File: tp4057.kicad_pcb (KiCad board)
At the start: 2 copper layers, 62.7 x 33.3 mm, 28 parts, among them J1 Conn_02x01, J2 Conn_02x01, J3 USB_C_Receptacle_PowerOnly_6P, J4 Conn_02x01, U1 TP4057, U2 TP4057, U3 TP4057

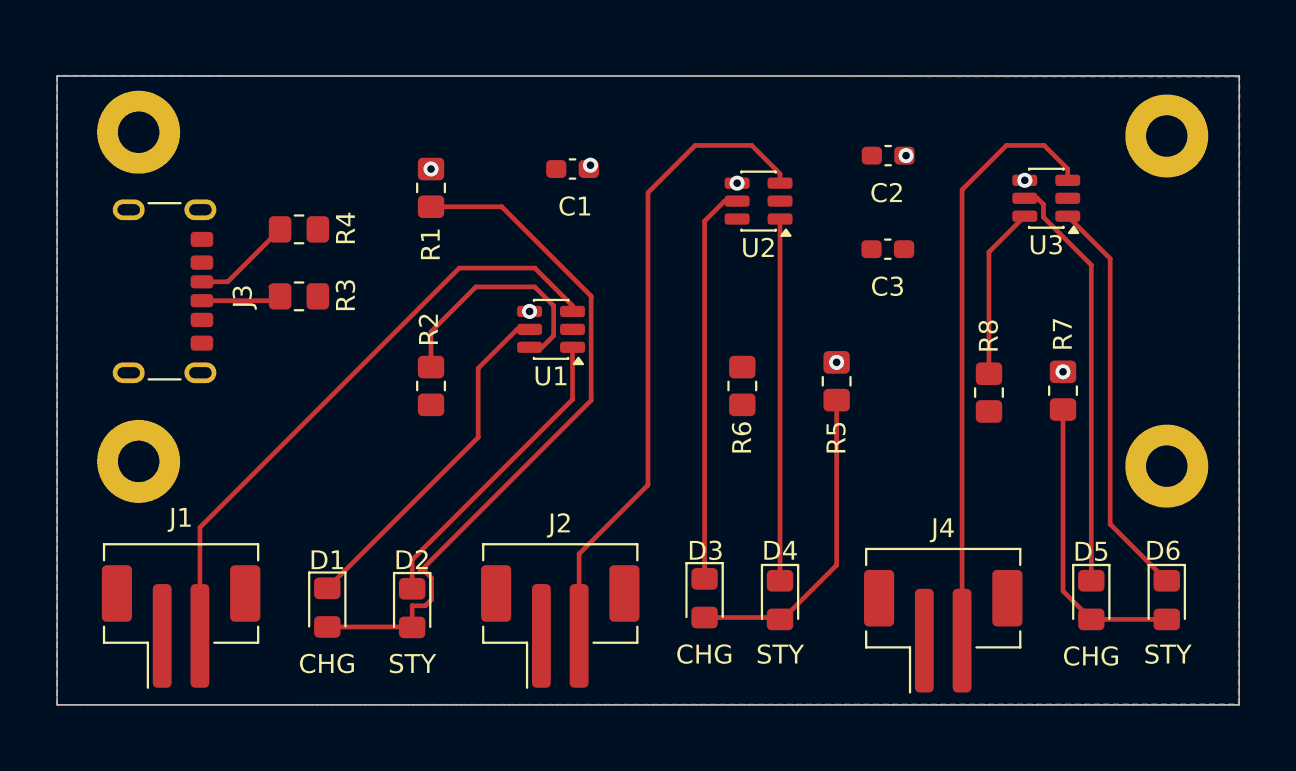
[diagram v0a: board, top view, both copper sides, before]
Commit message: Fixed VCC plane not connecting (misplaced vias), changed trace thickness, routed remaining components
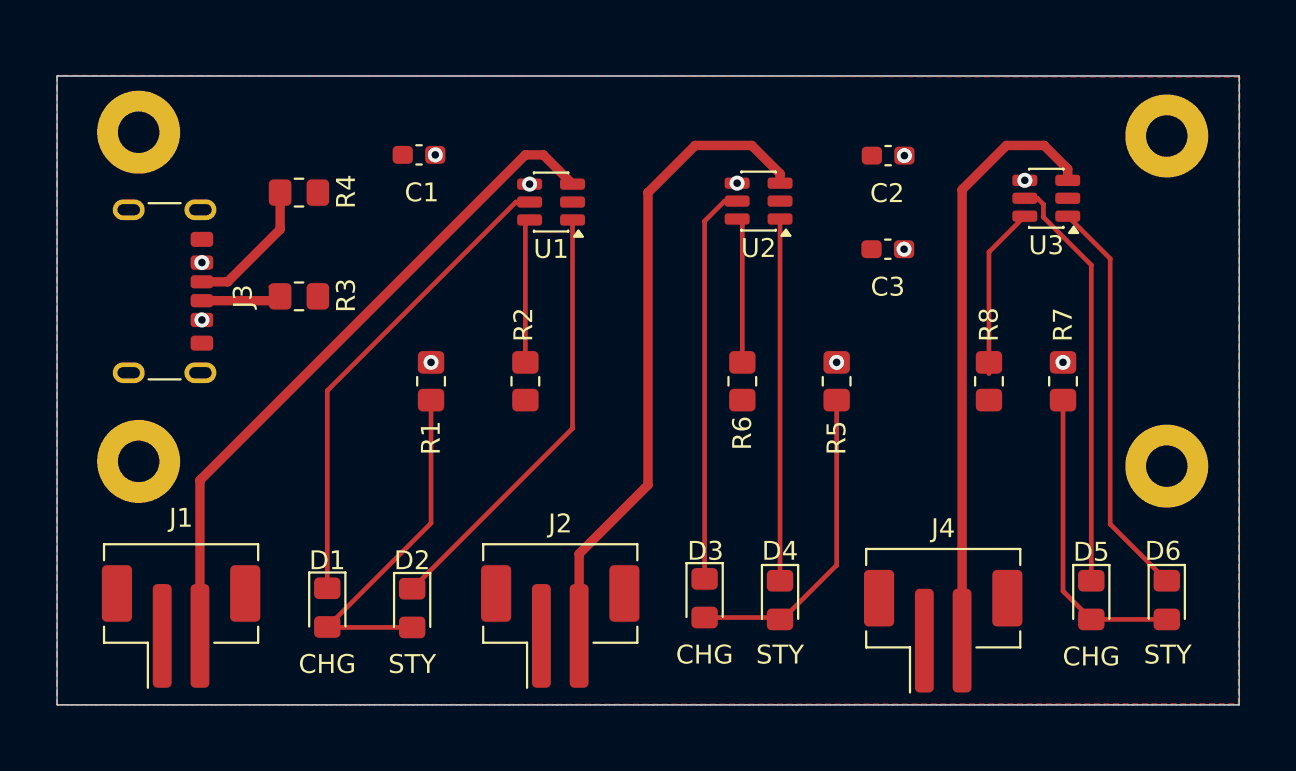
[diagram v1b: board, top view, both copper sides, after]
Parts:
- moved R1 10.2 mm to (158.0, 134.5)
- moved C1 8.17 mm to (157.4, 122.5)
- moved U1 6.75 mm to (164.4, 125.0)
- moved R2 5.01 mm to (163.0, 134.5)
- moved R4 1.95 mm to (151.0, 124.5)
- moved R8 0.60 mm to (187.6, 134.5)
- moved R7 0.50 mm to (191.5, 134.5)
- moved R6 0.25 mm to (174.5, 134.5)
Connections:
- H1 pad 1: GND -> unconnected-(H1-Pad1)
- H2 pad 1: GND -> unconnected-(H2-Pad1)
- H3 pad 1: GND -> unconnected-(H3-Pad1)
- H4 pad 1: GND -> unconnected-(H4-Pad1)
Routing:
- net Net-(D1-A): track 37.6 -> 18.8 mm
- net Net-(U2-PROG): track 0.00 -> 7.96 mm
- net Net-(D1-K): track 18.6 -> 25.3 mm
- net Net-(D2-K): track 16.3 -> 23.1 mm
- net Net-(U1-PROG): track 13.5 -> 7.64 mm
- net Net-(J1-Pin_2): track 32.3 -> 35.8 mm
- net Net-(J3-CC1): track 5.30 -> 7.25 mm
- net VCC: vias 8 -> 11

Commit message: Board layout; new 3D JST footprint; added silkscreen
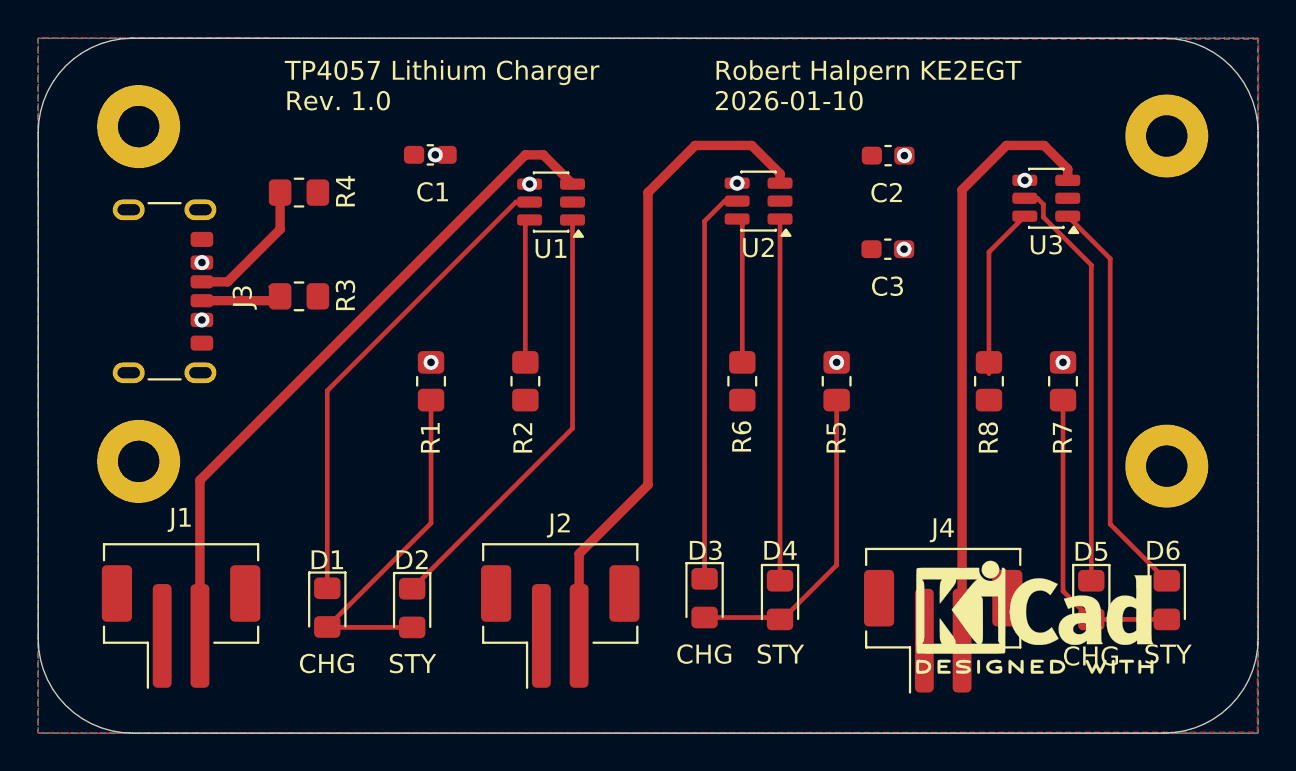
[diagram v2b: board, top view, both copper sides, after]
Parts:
- added REF**: KiCad-Logo2_5mm_SilkScreen, Symbol:KiCad-Logo2_5mm_SilkScreen, F.Cu at (190.0, 147.0)
- moved C1 0.60 mm to (158.0, 122.5)
- moved H1 0.30 mm to (142.5, 121.0)
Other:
- board size 62.7 x 33.3 mm -> 64.7 x 36.8 mm
- board text added: "${COMPANY} ${ISSUE_DATE}"
- board text added: "${TITLE} Rev. ${REVISION}"
